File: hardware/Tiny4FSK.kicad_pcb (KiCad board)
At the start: 4 copper layers, 35.1 x 76.3 mm, 90 parts, among them J1 Power Ext, J2 GPIO, J3 I2C, J4 USB, J5 USB Breakout, J6 SPI, J7 USBC, J8 SWD, J9 Counterpoise, SW1 Power Switch, SW2 RST, U1 BME280, U2 ATGM336H, U3 TPS61200DRC, U4 ECS-327TXO-2012, U5 ATSAMD21G18A-A, U6 SI4063, U7 Linear Step-Down

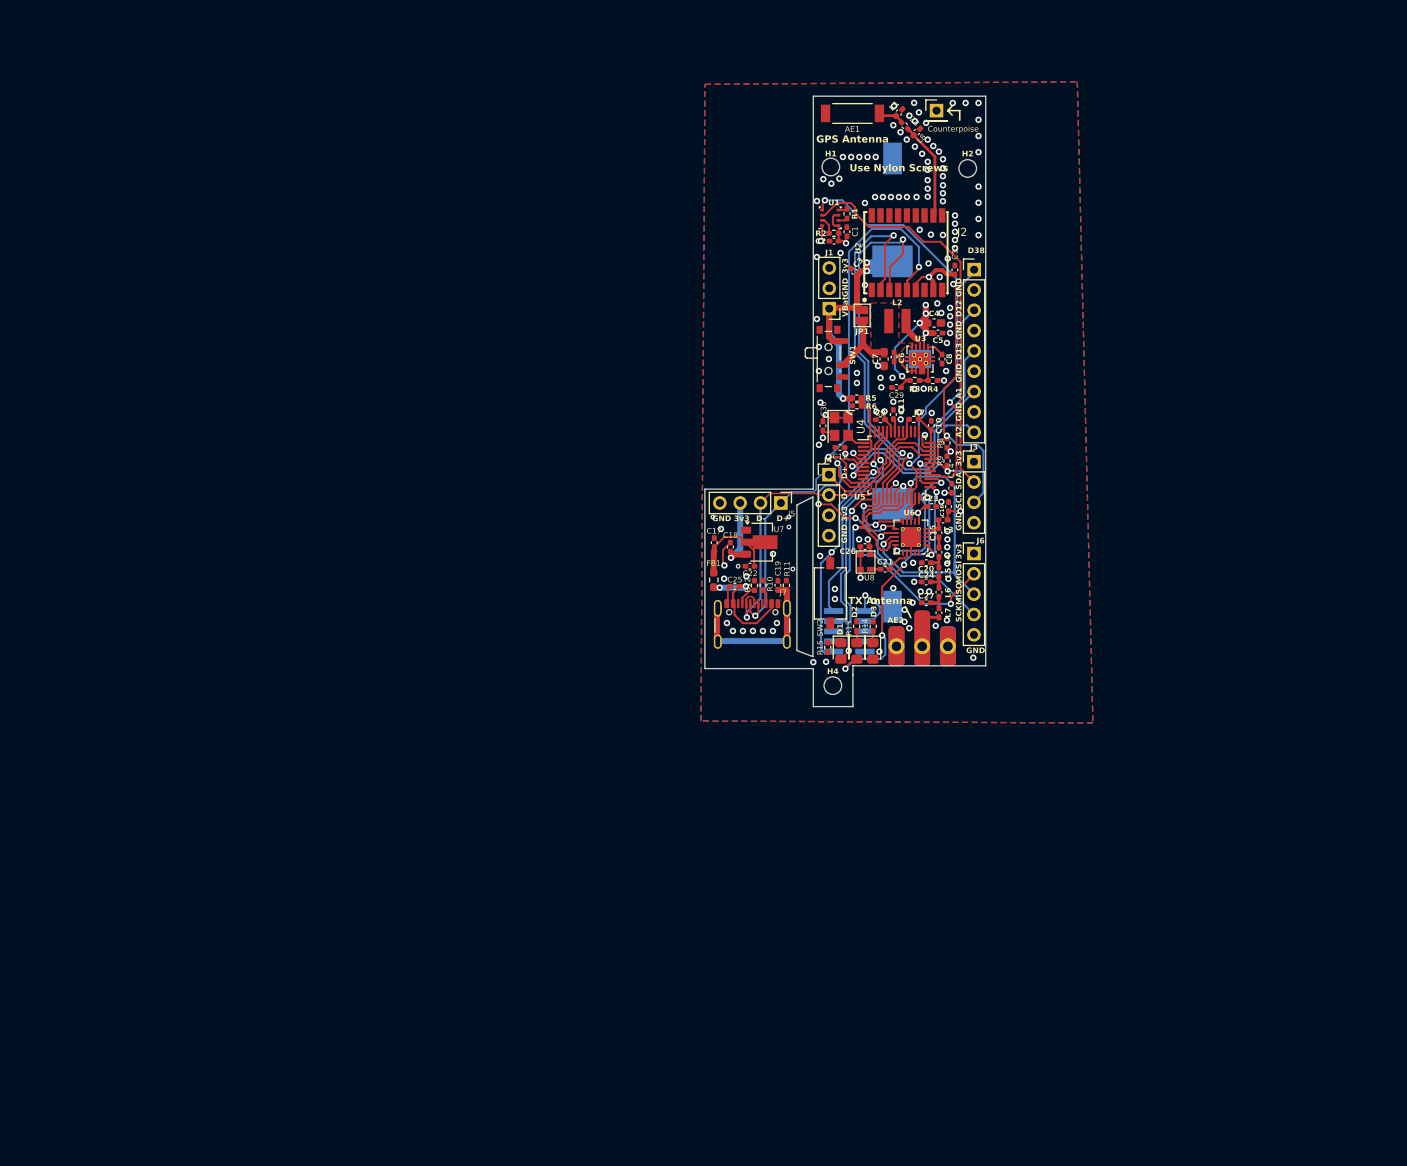
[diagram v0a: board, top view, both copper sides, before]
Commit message: pcb rework -- layout subsections and rough floorplanning
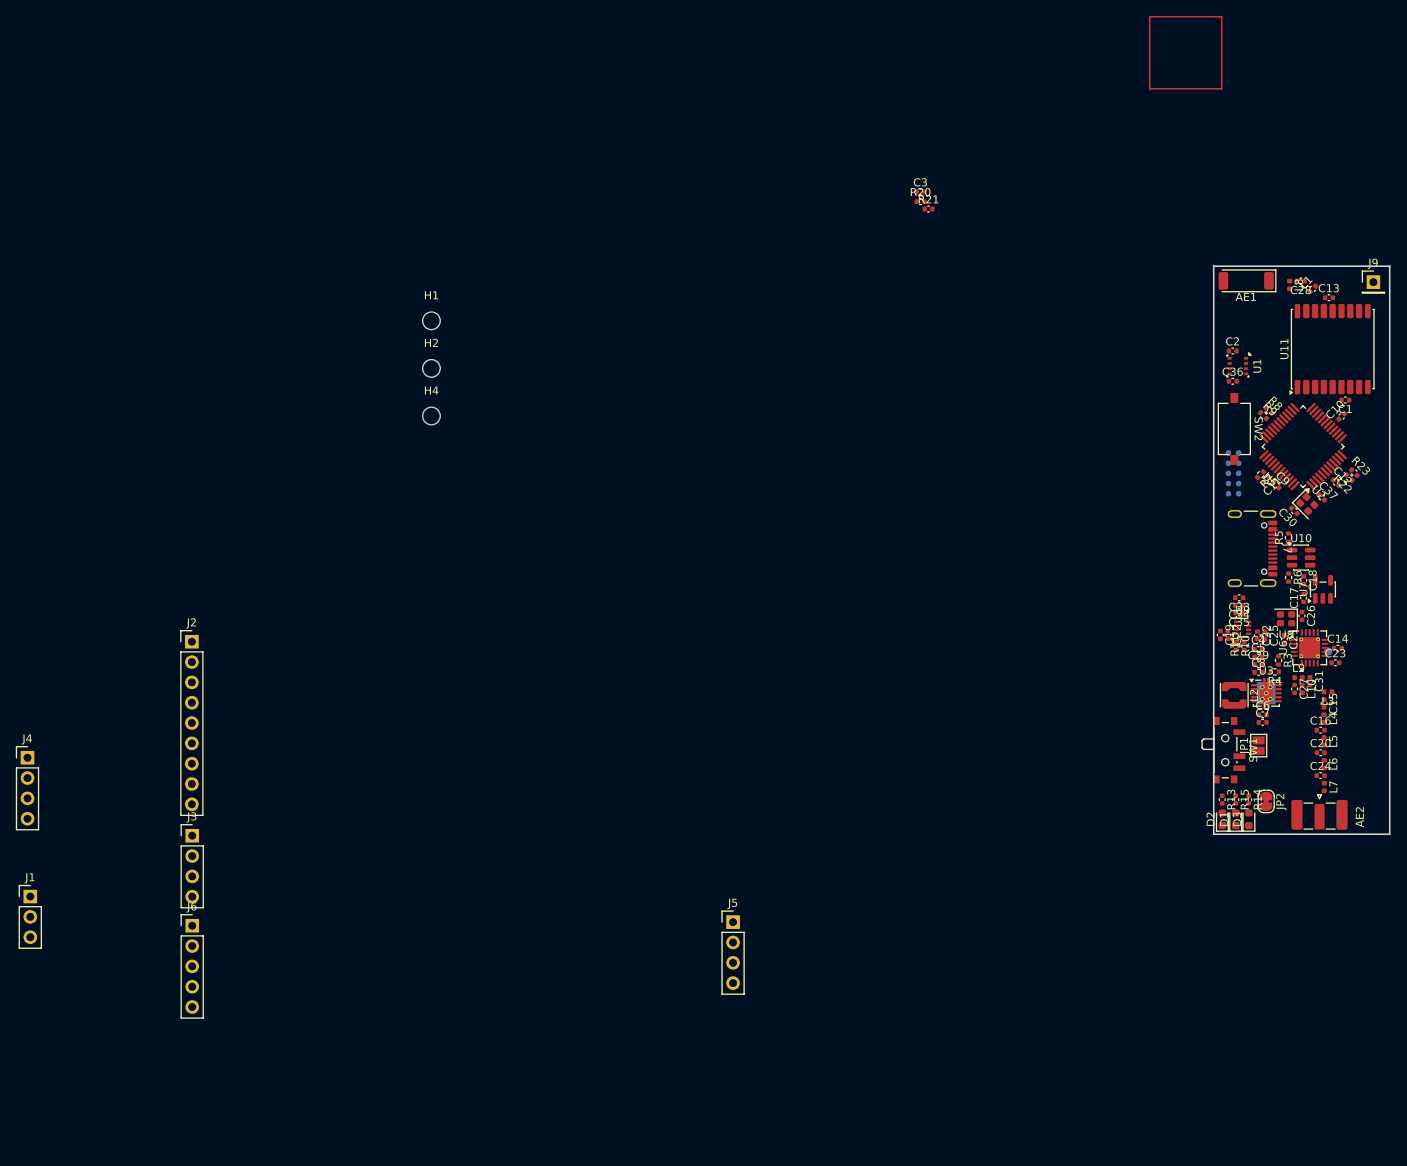
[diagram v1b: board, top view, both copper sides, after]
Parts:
- removed BT1: BK-53, BatteryExtended:BAT_53
- removed FB1: BLM18AG121SN1D, Resistor_SMD:R_0603_1608Metric_Pad0.98x0.95mm_HandSolder
- removed G*** (x7): LOGO, LOGO
- removed R1, R2: 10k, Resistor_SMD:R_0402_1005Metric_Pad0.72x0.64mm_HandSolder
- removed R12: 5k1, Resistor_SMD:R_0402_1005Metric_Pad0.72x0.64mm_HandSolder
- removed U4: ECS-327TXO-2012, Crystal:Crystal_SMD_3225-4Pin_3.2x2.5mm
- added C31: 3.9pF, Capacitor_SMD:C_0402_1005Metric, F.Cu at (202.4, 110.0)
- added C32: 100nF, Capacitor_SMD:C_0402_1005Metric, F.Cu at (195.8, 104.3)
- added C33: 100nF, Capacitor_SMD:C_0402_1005Metric, F.Cu at (193.5, 99.6)
- added C34: 1uF, Capacitor_SMD:C_0402_1005Metric, F.Cu at (193.5, 100.5)
- added C35: 100uF, Capacitor_SMD:C_0402_1005Metric, F.Cu at (193.5, 101.5)
- added C36: 100nF, Capacitor_SMD:C_0402_1005Metric, F.Cu at (192.7, 72.5)
- added C37: 100nF, Capacitor_SMD:C_0402_1005Metric, F.Cu at (203.8, 87.0)
- added JP2: POWER_LED_ENABLE, Jumper:SolderJumper-2_P1.3mm_Bridged_RoundedPad1.0x1.5mm, F.Cu at (196.9, 125.1)
- added L10: 51nH, Inductor_SMD:L_0402_1005Metric, F.Cu at (201.4, 111.0)
- added L9: 56nH, Inductor_SMD:L_0402_1005Metric, F.Cu at (200.9, 109.6)
- added R20: 100kR, Capacitor_SMD:C_0402_1005Metric, F.Cu at (153.7, 50.1)
- added R21: 150kR, Capacitor_SMD:C_0402_1005Metric, F.Cu at (154.7, 51.0)
- added R22: 100kR, Capacitor_SMD:C_0402_1005Metric, F.Cu at (207.3, 84.6)
- added R23: 150kR, Capacitor_SMD:C_0402_1005Metric, F.Cu at (207.9, 84.0)
- added TP1: ExtPA, TestPoint:TestPoint_Pad_D1.0mm, B.Cu at (204.7, 106.3)
- added U10: USBLC6-2SC6, Package_TO_SOT_SMD:SOT-23-6, F.Cu at (201.3, 94.6)
- added U11: ATGM336H, RF_GPS:ublox_MAX, F.Cu at (205.2, 68.5)
- added U9: TPS2116DRL, Package_TO_SOT_SMD:SOT-583-8, F.Cu at (194.0, 103.3)
- AE1: footprint RF_Antenna_Extended:ANT_1575AT_JOT -> RF_Antenna:Johanson_2450AT43F0100_2400-2500Mhz
- AE2: footprint Antenna:Antenna_Whip -> Connector_Coaxial:SMA_Samtec_SMA-J-P-H-ST-EM1_EdgeMount
- C1, C11, C13, C14, C18, C23, C29, C5, C8, C9: footprint Capacitor_SMD:C_0402_1005Metric_Pad0.74x0.62mm_HandSolder -> Capacitor_SMD:C_0402_1005Metric
- C10, C26, C30, C6: value 100 nF -> 100nF; footprint Capacitor_SMD:C_0402_1005Metric_Pad0.74x0.62mm_HandSolder -> Capacitor_SMD:C_0402_1005Metric
- C12: value 10 uF -> 10uF; footprint Capacitor_SMD:C_0402_1005Metric_Pad0.74x0.62mm_HandSolder -> Capacitor_SMD:C_0402_1005Metric
- C15: value 9.1 pF -> 9.1pF; footprint Capacitor_SMD:C_0402_1005Metric_Pad0.74x0.62mm_HandSolder -> Capacitor_SMD:C_0402_1005Metric
- C16: value 100nF -> 13pF; footprint Capacitor_SMD:C_0402_1005Metric_Pad0.74x0.62mm_HandSolder -> Capacitor_SMD:C_0402_1005Metric
- C17, C25: value 100 nF -> 1uF; footprint Capacitor_SMD:C_0402_1005Metric_Pad0.74x0.62mm_HandSolder -> Capacitor_SMD:C_0402_1005Metric
- C19: value 4.7 nF -> 1uF; footprint Capacitor_SMD:C_0402_1005Metric_Pad0.74x0.62mm_HandSolder -> Capacitor_SMD:C_0402_1005Metric
- C2, C22: value 1uF -> 100nF; footprint Capacitor_SMD:C_0402_1005Metric_Pad0.74x0.62mm_HandSolder -> Capacitor_SMD:C_0402_1005Metric
- C20: value 8 pF -> 10pF; footprint Capacitor_SMD:C_0402_1005Metric_Pad0.74x0.62mm_HandSolder -> Capacitor_SMD:C_0402_1005Metric
- C21: value 100 pF -> 100nF; footprint Capacitor_SMD:C_0402_1005Metric_Pad0.74x0.62mm_HandSolder -> Capacitor_SMD:C_0402_1005Metric
- C24: value 6 pF -> 10pF; footprint Capacitor_SMD:C_0402_1005Metric_Pad0.74x0.62mm_HandSolder -> Capacitor_SMD:C_0402_1005Metric
- C27: value 5 pF -> 2.2pF; footprint Capacitor_SMD:C_0402_1005Metric_Pad0.74x0.62mm_HandSolder -> Capacitor_SMD:C_0402_1005Metric
- C28: value 2.7pF -> 1.3pF; footprint Capacitor_SMD:C_0402_1005Metric_Pad0.74x0.62mm_HandSolder -> Capacitor_SMD:C_0402_1005Metric
- C3: value 1uF -> 10uF; footprint Capacitor_SMD:C_0402_1005Metric_Pad0.74x0.62mm_HandSolder -> Capacitor_SMD:C_0402_1005Metric
- C4: footprint Capacitor_SMD:C_0603_1608Metric_Pad1.08x0.95mm_HandSolder -> Capacitor_SMD:C_0402_1005Metric
- C7: value 10 uF -> 10uF; footprint Capacitor_SMD:C_0603_1608Metric_Pad1.08x0.95mm_HandSolder -> Capacitor_SMD:C_0402_1005Metric
- D1: value Success -> GOOD_LED; footprint LED_SMD:LED_0805_2012Metric_Pad1.15x1.40mm_HandSolder -> LED_SMD:LED_0603_1608Metric
- D2: value Error -> ERR_LED; footprint LED_SMD:LED_0805_2012Metric_Pad1.15x1.40mm_HandSolder -> LED_SMD:LED_0603_1608Metric
- D3: value Power -> PWR_LED; footprint LED_SMD:LED_0805_2012Metric_Pad1.15x1.40mm_HandSolder -> LED_SMD:LED_0603_1608Metric
- J1: value Power Ext -> EXT_PWR
- J7: value USBC -> GCT-4105
- J8: footprint Connector_PinHeader_1.27mm:PinHeader_2x05_P1.27mm_Vertical_SMD -> Connector_Pogo_1.27mm:Pogo_2x05_P1.27mm
- L1: value 3.9 nH -> 20nH; footprint Inductor_SMD:L_0402_1005Metric_Pad0.77x0.64mm_HandSolder -> Capacitor_SMD:C_0402_1005Metric
- L2: footprint IND_CONT:LPS3015222MRB -> Inductor_SMD:L_Coilcraft_LPS3010
- L3: value 220 nH -> 220nH; footprint Inductor_SMD:L_0402_1005Metric_Pad0.77x0.64mm_HandSolder -> Inductor_SMD:L_0402_1005Metric
- L4: value 14 nH -> 22nH; footprint Inductor_SMD:L_0402_1005Metric_Pad0.77x0.64mm_HandSolder -> Inductor_SMD:L_0402_1005Metric
- L5, L7: value 14 nH -> 21nH; footprint Inductor_SMD:L_0402_1005Metric_Pad0.77x0.64mm_HandSolder -> Inductor_SMD:L_0402_1005Metric
- L6: value 14 nH -> 36.5nH; footprint Inductor_SMD:L_0402_1005Metric_Pad0.77x0.64mm_HandSolder -> Inductor_SMD:L_0402_1005Metric
- L8: value 3.9 nH -> NC; footprint Inductor_SMD:L_0402_1005Metric_Pad0.77x0.64mm_HandSolder -> Inductor_SMD:L_0402_1005Metric
- R10: value 5k1 -> 10kR; footprint Resistor_SMD:R_0402_1005Metric_Pad0.72x0.64mm_HandSolder -> Resistor_SMD:R_0402_1005Metric
- R11: value 1M -> 5kR; footprint Resistor_SMD:R_0402_1005Metric_Pad0.72x0.64mm_HandSolder -> Resistor_SMD:R_0402_1005Metric
- R13, R14, R15: value 330 -> 330R; footprint Resistor_SMD:R_0402_1005Metric_Pad0.72x0.64mm_HandSolder -> Capacitor_SMD:C_0402_1005Metric
- R3: value 1M -> 1MR; footprint Resistor_SMD:R_0402_1005Metric_Pad0.72x0.64mm_HandSolder -> Resistor_SMD:R_0402_1005Metric
- R4: value 180k -> 180kR; footprint Resistor_SMD:R_0402_1005Metric_Pad0.72x0.64mm_HandSolder -> Resistor_SMD:R_0402_1005Metric
- R5, R6: value 1M -> 5.1kR; footprint Resistor_SMD:R_0402_1005Metric_Pad0.72x0.64mm_HandSolder -> Resistor_SMD:R_0402_1005Metric
- R7: value 220 -> 220R; footprint Resistor_SMD:R_0402_1005Metric_Pad0.72x0.64mm_HandSolder -> Resistor_SMD:R_0402_1005Metric
- R8, R9: value 1.8k -> 1.8kR; footprint Resistor_SMD:R_0402_1005Metric_Pad0.72x0.64mm_HandSolder -> Resistor_SMD:R_0402_1005Metric
- SW1: value Power Switch -> PWR
- U2: value ATGM336H -> ~; footprint RF_GPS_Extended:ATGM336H -> Crystal:Crystal_SMD_2016-4Pin_2.0x1.6mm
- U6: value SI4063 -> Si4463; footprint Package_DFN_QFN:QFN-20-1EP_4x4mm_P0.5mm_EP2.5x2.5mm_ThermalVias -> Package_DFN_QFN:QFN-20-1EP_4x4mm_P0.5mm_EP2.6x2.6mm_ThermalVias
- U7: value Linear Step-Down -> XC6210B332MR; footprint LDO:MCP1700 -> Package_TO_SOT_SMD:SOT-23-5
- U8: footprint Oscillator_TCXO:ECS-TXO-20CSMV4 -> Crystal:Crystal_SMD_2016-4Pin_2.0x1.6mm
- moved J1 124.0 mm to (42.4, 136.9), turned to 0 degrees
- moved J3 108.3 mm to (62.7, 129.3)
- moved J2 108.3 mm to (62.6, 105.1)
- moved J6 108.2 mm to (62.7, 140.6)
- moved J4 106.2 mm to (42.1, 119.6)
- moved C17 74.0 mm to (201.6, 99.6)
- moved JP1 73.1 mm to (196.0, 118.1)
- moved C18 71.8 mm to (201.6, 97.4), turned to -90 degrees
- moved H2 71.5 mm to (92.6, 70.9)
- moved U7 70.7 mm to (204.0, 98.5), turned to 90 degrees
- moved SW1 69.7 mm to (192.1, 118.7)
- moved C25 66.5 mm to (196.7, 104.3), turned to -90 degrees
- moved C1 65.8 mm to (206.8, 74.9), turned to 180 degrees
- moved C7 65.6 mm to (196.5, 115.2), turned to 0 degrees
- moved C6 64.2 mm to (196.5, 114.2), turned to 0 degrees
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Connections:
- net A1 renamed /interface/GP.GPIO_A_1
- net A2 renamed /interface/GP.GPIO_A_2
- net D12 renamed /interface/GP.GPIO12
- net D13 renamed /interface/GP.GPIO13
- net D38 renamed /interface/GP.GPIO38
- net GPIO0 renamed /mcu/SI.GP0
- net Net-(U6-XIN) renamed /radio/RF_XO
- net RF_RST renamed /mcu/SI.RST
- net RF_SS renamed /interface/GP.~{CS}
- net RF_XO renamed Net-(U8-OUT)
- net SCK renamed /interface/GP.CLK
- net SDN renamed /mcu/SI.SDN
- net SWCLK renamed /interface/PROG.SWCLK
- net SWDIO renamed /interface/PROG.SWDIO
- net nRST renamed /interface/PROG.~{RESET}
- C15 pad 1: RF_ANT -> /radio/SI_TX
- C16 pad 2: +3.3V -> Net-(C16-Pad2)
- C17 pad 1: LIN -> /power/USB_VBUS
- C18 pad 1: +3.3V -> /power/USB_3V3
- C19 pad 1: Earth -> /power/USB_3V3
- C19 pad 2: Net-(J7-SHIELD) -> Earth
- C20 pad 1: Net-(C20-Pad1) -> Earth
- C20 pad 2: Earth -> Net-(C20-Pad2)
- C22 pad 1: Earth -> /power/USB_3V3
- C22 pad 2: LIN -> Earth
- C24 pad 1: Net-(C24-Pad1) -> Earth
- C24 pad 2: Earth -> Net-(C24-Pad2)
- C25 pad 1: USB -> /power/BATT_3V3
- C27 pad 1: Net-(C27-Pad1) -> /radio/RX+
- C27 pad 2: Earth -> /radio/SI_TX
- C28 pad 1: ANT_GPS -> /sensors/ANT_GPS
- C29 pad 1: +3.3V -> /power/BATT_3V3
- C4 pad 1: +3.3V -> /power/BATT_3V3
- C5 pad 1: +3.3V -> /power/BATT_3V3
- C6 pad 1: BST_IN -> /power/BST_IN
- C7 pad 1: BST_IN -> /power/BST_IN
- C9 pad 1: Earth -> Net-(U5-VDDCORE)
- D1 pad 1: Net-(D1-K) -> Earth
- D1 pad 2: SUCCESS -> Net-(D1-A)
- D2 pad 1: Net-(D2-K) -> Earth
- D2 pad 2: ERROR -> Net-(D2-A)
- D3 pad 1: Net-(D3-K) -> Earth
- D3 pad 2: +3.3V -> Net-(D3-A)
- J3 pad 2: SDA -> /interface/GP.SDA
- J3 pad 3: SCL -> /interface/GP.SCL
- J4 pad 1: D+ -> /interface/GP.D+
- J4 pad 2: D- -> /interface/GP.D-
- J5 pad 1: D+ -> /interface/GP.D+
- J5 pad 2: D- -> /interface/GP.D-
- J5 pad 3: +3.3V -> /power/USB_3V3
- J6 pad 2: MOSI -> /interface/GP.MOSI
- J6 pad 3: MISO -> /interface/GP.MISO
- J7 pad A4: USB -> /power/USB_VBUS
- J7 pad A6: D+ -> Net-(J7-D+-PadA6)
- J7 pad A7: D- -> Net-(J7-D--PadA7)
- J7 pad A9: USB -> /power/USB_VBUS
- J7 pad B4: USB -> /power/USB_VBUS
- J7 pad B6: D+ -> Net-(J7-D+-PadA6)
- J7 pad B7: D- -> Net-(J7-D--PadA7)
- J7 pad B9: USB -> /power/USB_VBUS
- JP1 pad 1: BST_IN -> +BATT
- JP1 pad 2: +BATT -> /power/BST_IN
- L1 pad 2: Net-(AE1-A) -> /sensors/ANT_GPS
- L2 pad 2: BST_IN -> /power/BST_IN
- L3 pad 2: RF_ANT -> /radio/SI_TX
- L4 pad 2: Net-(C20-Pad1) -> Net-(C16-Pad2)
- L5 pad 1: Net-(C20-Pad1) -> Net-(C16-Pad2)
- L5 pad 2: Net-(C24-Pad1) -> Net-(C20-Pad2)
- L6 pad 1: Net-(C24-Pad1) -> Net-(C20-Pad2)
- L6 pad 2: Net-(C27-Pad1) -> Net-(C24-Pad2)
- L7 pad 1: Net-(C27-Pad1) -> Net-(C24-Pad2)
- L8 pad 1: Earth -> Net-(AE1-A)
- L8 pad 2: ANT_GPS -> Earth
- R10 pad 1: Earth -> Net-(U9-PR1)
- R10 pad 2: Net-(J7-CC2) -> /power/USB_3V3
- R11 pad 1: Net-(J7-SHIELD) -> Earth
- R11 pad 2: Earth -> Net-(U9-PR1)
- R13 pad 1: Net-(D2-K) -> /interface/LED.SUCCESS
- R13 pad 2: Earth -> Net-(D2-A)
- R14 pad 1: Net-(D3-K) -> Net-(JP2-A)
- R14 pad 2: Earth -> Net-(D3-A)
- R15 pad 1: Net-(D1-K) -> /interface/LED.ERROR
- R15 pad 2: Earth -> Net-(D1-A)
- R3 pad 1: +3.3V -> /power/BATT_3V3
- R5 pad 1: +BATT -> Net-(J7-CC1)
- R5 pad 2: BATT_SENSE -> Earth
- R6 pad 1: BATT_SENSE -> Net-(J7-CC2)
- R8 pad 2: SCL -> /interface/GP.SDA
- R9 pad 1: SDA -> +3.3V
- R9 pad 2: +3.3V -> /interface/GP.SCL
- SW1 pad 1: +BATT -> /power/BST_IN
- SW1 pad 2: BST_IN -> +BATT
- U1 pad 2: Net-(U1-CSB) -> +3.3V
- U1 pad 3: SDA -> /interface/GP.SDA
- U1 pad 4: SCL -> /interface/GP.SCL
- U1 pad 5: Net-(U1-SDO) -> Earth
- U2 pad 1: Earth -> +3.3V
- U2 pad 2: RXD -> Earth
- U2 pad 3: TXD -> Net-(U2-OUT)
- U2 pad 4: unconnected-(U2-PPS-Pad4) -> +3.3V
- U3 pad 2: +3.3V -> /power/BATT_3V3
- U3 pad 5: BST_IN -> /power/BST_IN
- U3 pad 6: BST_IN -> /power/BST_IN
- U3 pad 7: BST_IN -> /power/BST_IN
- U5 pad 1: TCXO -> /mcu/SAMD_TCXO
- U5 pad 11: GPS_EN -> /mcu/GPS.EN
- U5 pad 13: SUCCESS -> /interface/LED.SUCCESS
- U5 pad 14: GPIO1 -> /mcu/SI_CTL.GP1
- U5 pad 15: TXD -> /mcu/TXD
- U5 pad 16: RXD -> /mcu/RXD
- U5 pad 19: MOSI -> /interface/GP.MOSI
- U5 pad 21: MISO -> /interface/GP.MISO
- U5 pad 24: ERROR -> /interface/LED.ERROR
- U5 pad 29: D6 -> unconnected-(U5-PA20-Pad29)
- U5 pad 3: BATT_SENSE -> /mcu/BATT_V
- U5 pad 30: D7 -> unconnected-(U5-PA21-Pad30)
- U5 pad 31: SDA -> /interface/GP.SDA
- U5 pad 32: SCL -> /interface/GP.SCL
- U5 pad 33: D- -> /interface/GP.D-
- U5 pad 34: D+ -> /interface/GP.D+
- U5 pad 9: unconnected-(U5-PA04-Pad9) -> /mcu/SUPP_V
- U6 pad 10: GPIO1 -> /mcu/SI.GP1
- U6 pad 13: MISO -> /interface/GP.MISO
- U6 pad 14: MOSI -> /interface/GP.MISO
- U6 pad 2: unconnected-(U6-NC_1-Pad2) -> /radio/RX+
- U6 pad 3: unconnected-(U6-NC_2-Pad3) -> /radio/RX-
- U6 pad 4: RF_ANT -> /radio/SI_TX
- U6 pad 7: unconnected-(U6-TXRAMP-Pad7) -> Net-(U6-TXRAMP)
- U7 pad 1: Earth -> /power/USB_VBUS
- U7 pad 2: +3.3V -> Earth
- U7 pad 3: LIN -> /power/USB_VBUS
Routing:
- net +3.3V: track 74.9 -> 0.00 mm, vias 20 -> 0
- net SCL: track 59.0 -> 0.00 mm, vias 3 -> 0
- net SDA: track 56.2 -> 0.00 mm, vias 1 -> 0
- net GPS_EN: track 50.3 -> 0.00 mm, vias 2 -> 0
- net RXD: track 49.4 -> 0.00 mm, vias 2 -> 0
- net TXD: track 47.2 -> 0.00 mm, vias 2 -> 0
- net D-: track 45.2 -> 0.00 mm, vias 1 -> 0
- net D+: track 45.1 -> 0.00 mm, vias 1 -> 0
- net Earth: track 41.2 -> 0.00 mm, vias 142 -> 0
- net +BATT: track 40.8 -> 0.00 mm, vias 3 -> 0
- net MOSI: track 39.2 -> 0.00 mm, vias 2 -> 0
- net /interface/PROG.~{RESET}: track 37.4 -> 0.00 mm, vias 2 -> 0
- net MISO: track 37.3 -> 0.00 mm, vias 2 -> 0
- net /interface/GP.GPIO38: track 32.8 -> 0.00 mm, vias 1 -> 0
- net ERROR: track 32.1 -> 0.00 mm, vias 4 -> 0
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- removed copper zone on In2.Cu, net +3.3V
- removed copper zone on F.Cu, net BST_IN
- removed copper zone on B.Cu, net Earth
- removed copper zone on F.Cu, net Earth
- removed copper zone on In1.Cu, net Earth
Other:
- board size 35.1 x 76.3 mm -> 22 x 71 mm
- board text removed: "+"
- board text removed: "-"
- board text removed: "04-2026"
- board text removed: "3v3"
- board text removed: "A1"
- board text removed: "A2"
- board text removed: "Counterpoise"
- board text removed: "D+"
- board text removed: "D-"
- board text removed: "D12"
- board text removed: "D13"
- board text removed: "D38"
- board text removed: "GND"
- board text removed: "GPS Antenna"
- board text removed: "Licensed under CERN-OHL-W-2.0"
- board text removed: "MISO"
- board text removed: "MOSI"
- board text removed: "Max Kendall W0MXX"
- board text removed: "Max W0MXX"
- board text removed: "Rev. 2.2"
- board text removed: "SCK"
- board text removed: "SCL"
- board text removed: "SDA"
- board text removed: "Sponsored by:"
- board text removed: "TX Antenna"
- board text removed: "USB Breakout"
- board text removed: "Use Nylon Screws"
- board text removed: "VBat"
- board text removed: "https://mpkendall.com/tiny4fsk"

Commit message: move button up
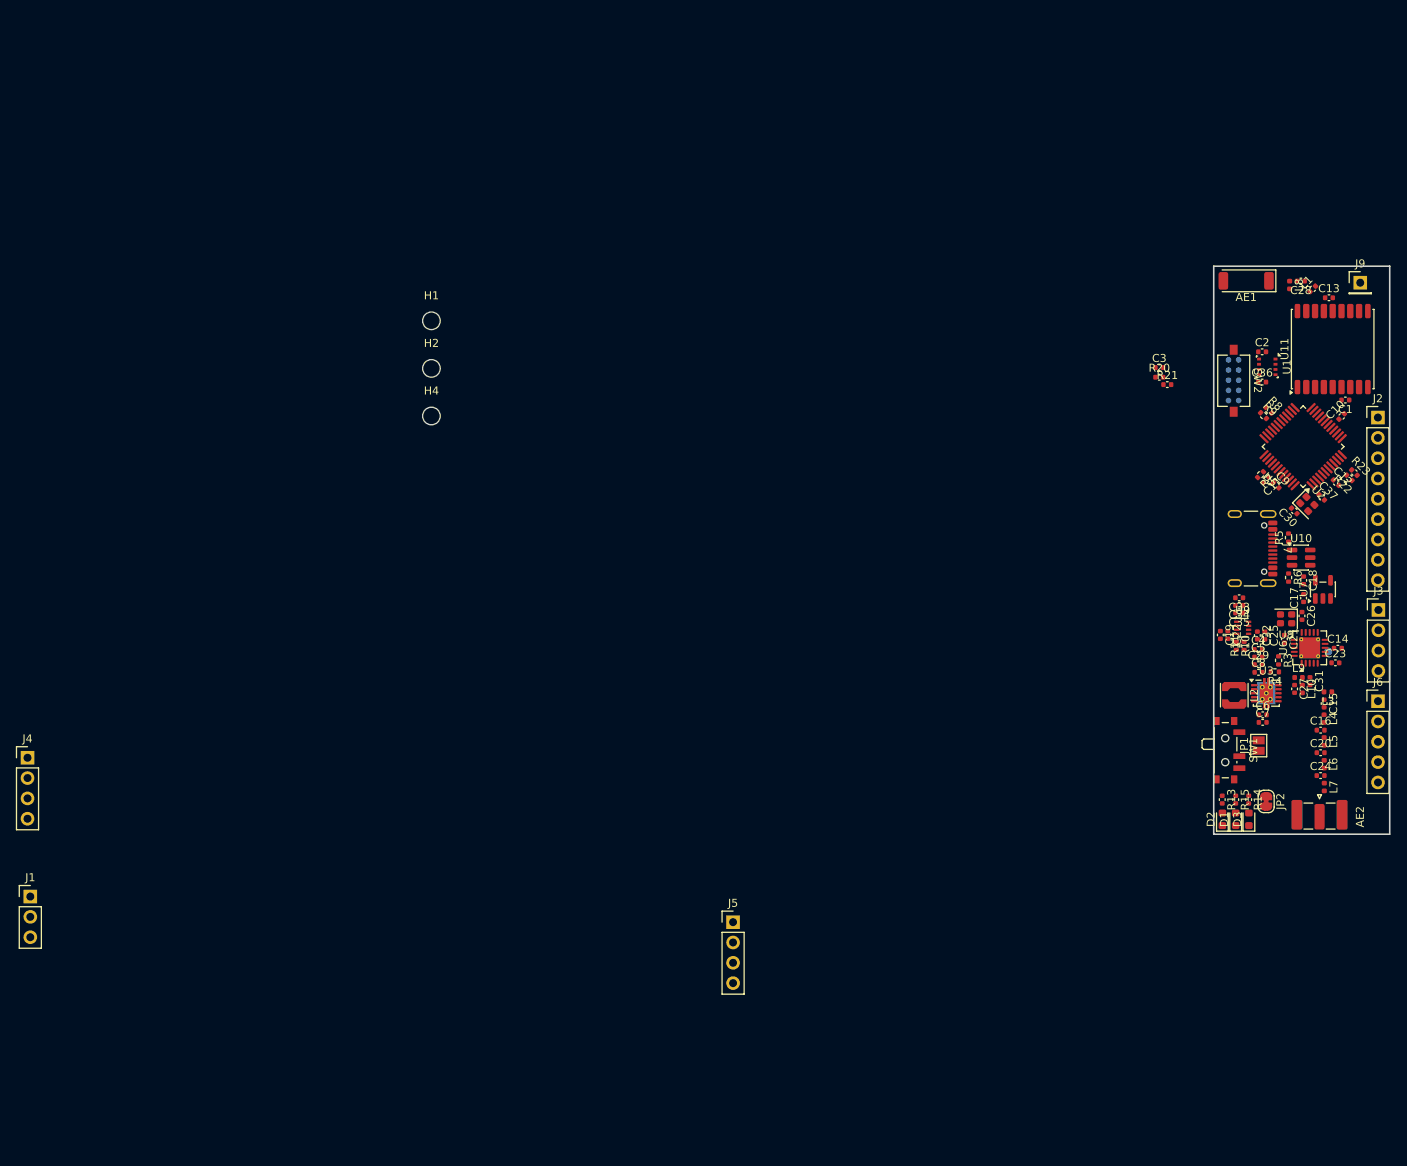
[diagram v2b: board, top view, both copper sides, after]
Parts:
- moved J3 150.9 mm to (210.9, 101.1)
- moved J2 150.9 mm to (210.9, 77.1)
- moved J6 150.9 mm to (210.9, 112.5)
- moved R20 37.1 mm to (183.6, 72.0)
- moved R21 37.1 mm to (184.6, 73.0)
- moved C3 37.1 mm to (183.6, 70.8)
- moved J8 11.6 mm to (192.8, 72.4)
- moved SW2 6.03 mm to (192.8, 72.5)
- moved C2 3.68 mm to (196.4, 68.8)
- moved C36 3.68 mm to (196.4, 72.6)
- moved U1 3.68 mm to (197.0, 70.7)
- moved J9 1.65 mm to (208.7, 60.2)
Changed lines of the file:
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@@
 	(footprint "Connector_PinHeader_2.54mm:PinHeader_1x09_P2.54mm_Vertical"
 		(layer "F.Cu")
-		(at 62.62 105.095)
+		(at 210.87 77.07)
 		(descr "Through hole straight pin header, 1x09, 2.54mm pitch, single row")
 		(tags "Through hole pin header THT 1x09 2.54mm single row")
@@
 	(footprint "Button_Switch_SMD:SW_Tactile_SPST_NO_Straight_CK_PTS636Sx25SMTRLFS"
 		(layer "F.Cu")
-		(at 192.925 78.495 -90)
+		(at 192.85 72.47 -90)
 		(descr "Tactile switch, SPST, 6.0x3.5 mm, H2.5 mm, straight, NO, gull wing leads: https://www.ckswitches.com/media/2779/pts636.pdf")
 		(tags "switch tactile SPST 1P1T straight NO SMTR C&K")
@@
 	(footprint "Capacitor_SMD:C_0402_1005Metric"
 		(layer "F.Cu")
-		(at 154.7 51)
+		(at 184.55 72.95)
 		(descr "Capacitor SMD 0402 (1005 Metric), square (rectangular) end terminal, IPC-7351 nominal, (Body size source: IPC-SM-782 page 76, https://www.pcb-3d.com/wordpress/wp-content/uploads/ipc-sm-782a_amendment_1_and_2.pdf)")
 		(tags "capacitor")
@@
 	(footprint "Connector_PinHeader_2.54mm:PinHeader_1x05_P2.54mm_Vertical"
 		(layer "F.Cu")
-		(at 62.66 140.595)
+		(at 210.885 112.52)
 		(descr "Through hole straight pin header, 1x05, 2.54mm pitch, single row")
 		(tags "Through hole pin header THT 1x05 2.54mm single row")
@@
 	(footprint "Capacitor_SMD:C_0402_1005Metric"
 		(layer "F.Cu")
-		(at 192.73 68.75)
+		(at 196.405 68.85)
 		(descr "Capacitor SMD 0402 (1005 Metric), square (rectangular) end terminal, IPC-7351 nominal, (Body size source: IPC-SM-782 page 76, https://www.pcb-3d.com/wordpress/wp-content/uploads/ipc-sm-782a_amendment_1_and_2.pdf)")
 		(tags "capacitor")
@@
 	(footprint "Connector_PinHeader_2.54mm:PinHeader_1x01_P2.54mm_Vertical"
 		(layer "F.Cu")
-		(at 210.315 60.14)
+		(at 208.665 60.215)
 		(descr "Through hole straight pin header, 1x01, 2.54mm pitch, single row")
 		(tags "Through hole pin header THT 1x01 2.54mm single row")
@@
 	(footprint "Capacitor_SMD:C_0402_1005Metric"
 		(layer "F.Cu")
-		(at 153.7 50.08)
+		(at 183.55 72.03)
 		(descr "Capacitor SMD 0402 (1005 Metric), square (rectangular) end terminal, IPC-7351 nominal, (Body size source: IPC-SM-782 page 76, https://www.pcb-3d.com/wordpress/wp-content/uploads/ipc-sm-782a_amendment_1_and_2.pdf)")
 		(tags "capacitor")
@@
 	(footprint "Capacitor_SMD:C_0402_1005Metric"
 		(layer "F.Cu")
-		(at 153.7 48.87)
+		(at 183.55 70.82)
 		(descr "Capacitor SMD 0402 (1005 Metric), square (rectangular) end terminal, IPC-7351 nominal, (Body size source: IPC-SM-782 page 76, https://www.pcb-3d.com/wordpress/wp-content/uploads/ipc-sm-782a_amendment_1_and_2.pdf)")
 		(tags "capacitor")
@@
 	(footprint "Connector_PinHeader_2.54mm:PinHeader_1x04_P2.54mm_Vertical"
 		(layer "F.Cu")
-		(at 62.66 129.345)
+		(at 210.935 101.12)
 		(descr "Through hole straight pin header, 1x04, 2.54mm pitch, single row")
 		(tags "Through hole pin header THT 1x04 2.54mm single row")
@@
 	(footprint "Package_LGA:Bosch_LGA-8_2.5x2.5mm_P0.65mm_ClockwisePinNumbering"
 		(layer "F.Cu")
-		(at 193.365 70.635 -90)
+		(at 197.04 70.735 -90)
 		(descr "LGA-8")
 		(tags "lga land grid array")
@@
 	(footprint "Capacitor_SMD:C_0402_1005Metric"
 		(layer "F.Cu")
-		(at 192.73 72.535)
+		(at 196.405 72.635)
 		(descr "Capacitor SMD 0402 (1005 Metric), square (rectangular) end terminal, IPC-7351 nominal, (Body size source: IPC-SM-782 page 76, https://www.pcb-3d.com/wordpress/wp-content/uploads/ipc-sm-782a_amendment_1_and_2.pdf)")
 		(tags "capacitor")
@@
 	(footprint "Connector_Pogo_1.27mm:Pogo_2x05_P1.27mm"
 		(layer "B.Cu")
-		(at 192.83 84.05)
+		(at 192.83 72.4)
 		(property "Reference" "J8"
 			(at -0.075 4.15 180)
@@
 	)
 	(gr_rect
-		(start 182.35 26.975)
-		(end 191.35 35.975)
-		(stroke
-			(width 0.2)
-			(type solid)
-		)
-		(fill no)
-		(layer "F.Cu")
-	)
-	(gr_rect
